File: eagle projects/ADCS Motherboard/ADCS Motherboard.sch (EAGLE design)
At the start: 141 parts, among them J1 HDR_10_EZFET_DEBUGGER, J11 CNC_3221-10-0300-00, J5 CNC_3221-10-0300-00, J7 TE-1734829-3, Q1 BSR802NL6327HTSA1, U1 MSP430F5529IPN, U10 TSV991AILT, U2 TSV991AILT, U3 ADS7841E_2K5, U4 TSV991AILT, U5 DMC4050SSDQ-13, U7 HMC1053, U9 BMX160, Y1 32.768kHz, Y2 CSTCR4M00G15L99, Y3 32.768kHz

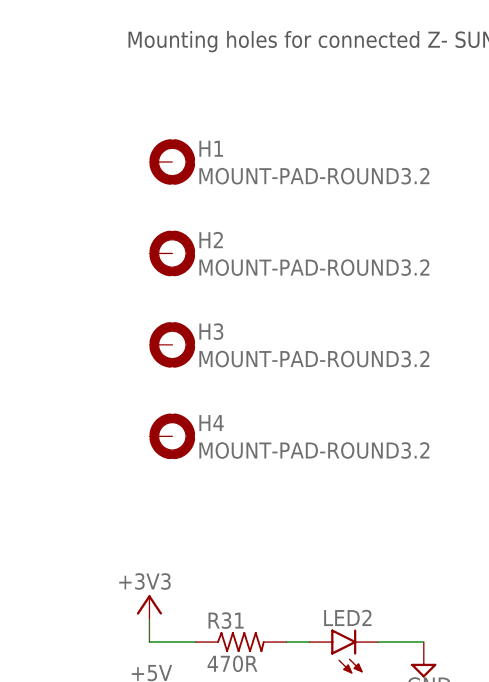
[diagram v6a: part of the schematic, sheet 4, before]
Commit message: Grounded standoff mounting hole pins
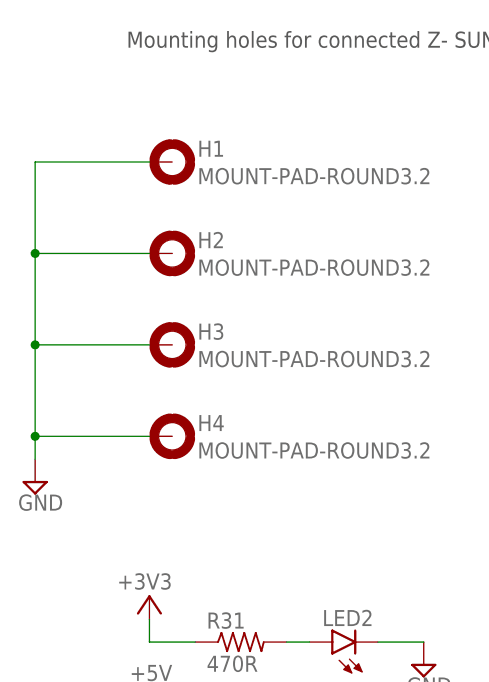
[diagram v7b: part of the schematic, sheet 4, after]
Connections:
- net GND: now also H1.MOUNT, H2.MOUNT, H3.MOUNT, H4.MOUNT
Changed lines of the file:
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@@
 <part name="JP1" library="pinhead" library_urn="urn:adsk.eagle:library:325" deviceset="PINHD-2X5" device="" package3d_urn="urn:adsk.eagle:package:22470/2"/>
 <part name="U5" library="my_library" library_urn="urn:adsk.eagle:library:22876504" deviceset="DMC4050SSDQ-13" device=""/>
+<part name="SUPPLY57" library="supply2" library_urn="urn:adsk.eagle:library:372" deviceset="GND" device=""/>
 </parts>
 <sheets>
@@
 <attribute name="NAME" x="142.24" y="88.9" size="1.2" layer="95" font="vector" ratio="10"/>
 </instance>
+<instance part="SUPPLY57" gate="GND" x="7.62" y="58.42" smashed="yes">
+<attribute name="VALUE" x="5.715" y="55.245" size="1.778" layer="96"/>
+</instance>
 </instances>
 <busses>
@@
 <pinref part="C33" gate="G$1" pin="2"/>
 </segment>
+<segment>
+<pinref part="SUPPLY57" gate="GND" pin="GND"/>
+<wire x1="7.62" y1="60.96" x2="7.62" y2="63.5" width="0.1524" layer="91"/>
+<pinref part="H1" gate="G$1" pin="MOUNT"/>
+<wire x1="7.62" y1="63.5" x2="7.62" y2="73.66" width="0.1524" layer="91"/>
+<wire x1="7.62" y1="73.66" x2="7.62" y2="83.82" width="0.1524" layer="91"/>
+<wire x1="7.62" y1="83.82" x2="7.62" y2="93.98" width="0.1524" layer="91"/>
+<wire x1="7.62" y1="93.98" x2="20.32" y2="93.98" width="0.1524" layer="91"/>
+<pinref part="H2" gate="G$1" pin="MOUNT"/>
+<wire x1="20.32" y1="83.82" x2="7.62" y2="83.82" width="0.1524" layer="91"/>
+<junction x="7.62" y="83.82"/>
+<pinref part="H3" gate="G$1" pin="MOUNT"/>
+<wire x1="20.32" y1="73.66" x2="7.62" y2="73.66" width="0.1524" layer="91"/>
+<junction x="7.62" y="73.66"/>
+<pinref part="H4" gate="G$1" pin="MOUNT"/>
+<wire x1="20.32" y1="63.5" x2="7.62" y2="63.5" width="0.1524" layer="91"/>
+<junction x="7.62" y="63.5"/>
+</segment>
 </net>

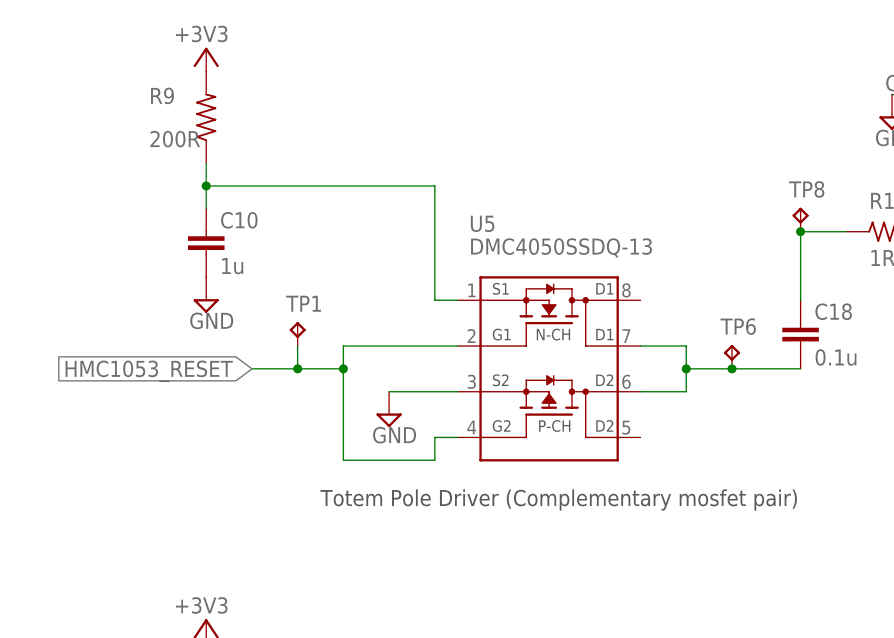
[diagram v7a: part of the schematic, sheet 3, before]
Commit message: stitching vias and silkscreen and fixed reversed totem pole driver (oops)
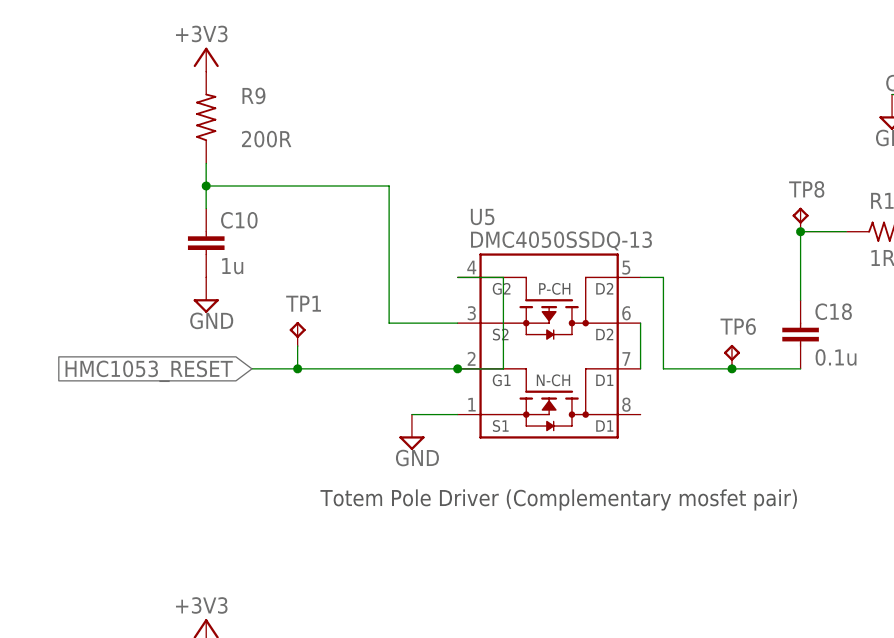
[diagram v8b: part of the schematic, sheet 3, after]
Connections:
- new net N$48: U5.D1_2, U5.D2_1
- net GND: now also U5.S1; no longer U5.S2
- net N$39: now also U5.S2; no longer U5.S1
- net N$9: now also U5.D2_2; no longer U5.D1_2, U5.D2_1
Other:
- moved on the sheet: U5
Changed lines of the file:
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@@
 <attribute name="VALUE" x="102.235" y="192.405" size="1.778" layer="96"/>
 </instance>
-<instance part="SUPPLY54" gate="GND" x="48.26" y="162.56" smashed="yes">
-<attribute name="VALUE" x="46.355" y="159.385" size="1.778" layer="96"/>
+<instance part="SUPPLY54" gate="GND" x="50.8" y="160.02" smashed="yes">
+<attribute name="VALUE" x="48.895" y="156.845" size="1.778" layer="96"/>
 </instance>
 <instance part="+3V24" gate="G$1" x="27.94" y="203.2" smashed="yes">
@@
 </instance>
 <instance part="R9" gate="G$1" x="27.94" y="195.58" smashed="yes" rot="R90">
-<attribute name="NAME" x="21.59" y="197.0786" size="1.778" layer="95"/>
-<attribute name="VALUE" x="21.59" y="192.278" size="1.778" layer="96"/>
+<attribute name="NAME" x="31.75" y="197.0786" size="1.778" layer="95"/>
+<attribute name="VALUE" x="31.75" y="192.278" size="1.778" layer="96"/>
 </instance>
 <instance part="C10" gate="G$1" x="27.94" y="180.34" smashed="yes" rot="R180">
@@
 <attribute name="VALUE" x="226.06" y="100.33" size="1.27" layer="96"/>
 </instance>
-<instance part="U5" gate="G$1" x="63.5" y="167.64" smashed="yes">
-<attribute name="VALUE" x="57.15" y="180.34" size="1.778" layer="96"/>
-<attribute name="NAME" x="57.15" y="182.88" size="1.778" layer="95"/>
+<instance part="U5" gate="G$1" x="63.5" y="170.18" smashed="yes" rot="MR180">
+<attribute name="VALUE" x="57.15" y="182.88" size="1.778" layer="96" rot="MR180"/>
+<attribute name="NAME" x="57.15" y="185.42" size="1.778" layer="95" rot="MR180"/>
 </instance>
 </instances>
@@
 </segment>
 <segment>
-<pinref part="U5" gate="G$1" pin="S2"/>
+<pinref part="U5" gate="G$1" pin="S1"/>
+<wire x1="55.88" y1="162.56" x2="50.8" y2="162.56" width="0.1524" layer="91"/>
 <pinref part="SUPPLY54" gate="GND" pin="GND"/>
-<wire x1="55.88" y1="165.1" x2="48.26" y2="165.1" width="0.1524" layer="91"/>
 </segment>
 </net>
@@
 <net name="HMC1053_RESET" class="0">
 <segment>
-<wire x1="43.18" y1="167.64" x2="38.1" y2="167.64" width="0.1524" layer="91"/>
 <wire x1="38.1" y1="170.18" x2="38.1" y2="167.64" width="0.1524" layer="91"/>
 <junction x="38.1" y="167.64"/>
@@
 <label x="33.02" y="167.64" size="1.778" layer="95" rot="R180" xref="yes"/>
 <pinref part="TP1" gate="G$1" pin="TP"/>
+<pinref part="U5" gate="G$1" pin="G1"/>
+<wire x1="38.1" y1="167.64" x2="55.88" y2="167.64" width="0.1524" layer="91"/>
 <pinref part="U5" gate="G$1" pin="G2"/>
-<wire x1="55.88" y1="160.02" x2="53.34" y2="160.02" width="0.1524" layer="91"/>
-<wire x1="43.18" y1="157.48" x2="43.18" y2="167.64" width="0.1524" layer="91"/>
-<junction x="43.18" y="167.64"/>
-<wire x1="43.18" y1="167.64" x2="43.18" y2="170.18" width="0.1524" layer="91"/>
-<pinref part="U5" gate="G$1" pin="G1"/>
-<wire x1="43.18" y1="170.18" x2="55.88" y2="170.18" width="0.1524" layer="91"/>
-<wire x1="43.18" y1="157.48" x2="53.34" y2="157.48" width="0.1524" layer="91"/>
-<wire x1="53.34" y1="157.48" x2="53.34" y2="160.02" width="0.1524" layer="91"/>
+<wire x1="55.88" y1="177.8" x2="60.96" y2="177.8" width="0.1524" layer="91"/>
+<wire x1="60.96" y1="177.8" x2="60.96" y2="167.64" width="0.1524" layer="91"/>
+<wire x1="60.96" y1="167.64" x2="55.88" y2="167.64" width="0.1524" layer="91"/>
+<junction x="55.88" y="167.64"/>
 </segment>
 </net>
@@
 <wire x1="27.94" y1="187.96" x2="27.94" y2="190.5" width="0.1524" layer="91"/>
 <junction x="27.94" y="187.96"/>
-<wire x1="53.34" y1="187.96" x2="27.94" y2="187.96" width="0.1524" layer="91"/>
-<pinref part="U5" gate="G$1" pin="S1"/>
-<wire x1="55.88" y1="175.26" x2="53.34" y2="175.26" width="0.1524" layer="91"/>
-<wire x1="53.34" y1="175.26" x2="53.34" y2="187.96" width="0.1524" layer="91"/>
+<pinref part="U5" gate="G$1" pin="S2"/>
+<wire x1="48.26" y1="187.96" x2="27.94" y2="187.96" width="0.1524" layer="91"/>
+<wire x1="55.88" y1="172.72" x2="48.26" y2="172.72" width="0.1524" layer="91"/>
+<wire x1="48.26" y1="172.72" x2="48.26" y2="187.96" width="0.1524" layer="91"/>
 </segment>
 </net>
@@
 <pinref part="TP6" gate="G$1" pin="TP"/>
 <wire x1="86.36" y1="167.64" x2="93.98" y2="167.64" width="0.1524" layer="91"/>
-<pinref part="U5" gate="G$1" pin="D1_2"/>
-<wire x1="76.2" y1="170.18" x2="81.28" y2="170.18" width="0.1524" layer="91"/>
-<wire x1="81.28" y1="170.18" x2="81.28" y2="167.64" width="0.1524" layer="91"/>
-<wire x1="81.28" y1="167.64" x2="86.36" y2="167.64" width="0.1524" layer="91"/>
+<pinref part="U5" gate="G$1" pin="D2_2"/>
+<wire x1="76.2" y1="177.8" x2="78.74" y2="177.8" width="0.1524" layer="91"/>
+<wire x1="78.74" y1="177.8" x2="78.74" y2="167.64" width="0.1524" layer="91"/>
+<wire x1="78.74" y1="167.64" x2="86.36" y2="167.64" width="0.1524" layer="91"/>
 <junction x="86.36" y="167.64"/>
-<wire x1="81.28" y1="167.64" x2="81.28" y2="165.1" width="0.1524" layer="91"/>
-<junction x="81.28" y="167.64"/>
-<pinref part="U5" gate="G$1" pin="D2_1"/>
-<wire x1="81.28" y1="165.1" x2="76.2" y2="165.1" width="0.1524" layer="91"/>
 </segment>
 </net>
@@
 </segment>
 </net>
+<net name="N$48" class="0">
+<segment>
+<pinref part="U5" gate="G$1" pin="D1_2"/>
+<wire x1="76.2" y1="167.64" x2="76.2" y2="172.72" width="0.1524" layer="91"/>
+<pinref part="U5" gate="G$1" pin="D2_1"/>
+</segment>
+</net>
